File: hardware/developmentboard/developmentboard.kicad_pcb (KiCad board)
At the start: 2 copper layers, 207.5 x 78.1 mm, 39 parts, among them J1 SPI Header, J2 Power Header, J3 Hall Effect Header, U1 ADS7960, U10 DRV5053, U11 DRV5053, U12 DRV5053, U13 DRV5053, U15 REF5025AD, U2 DRV5053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

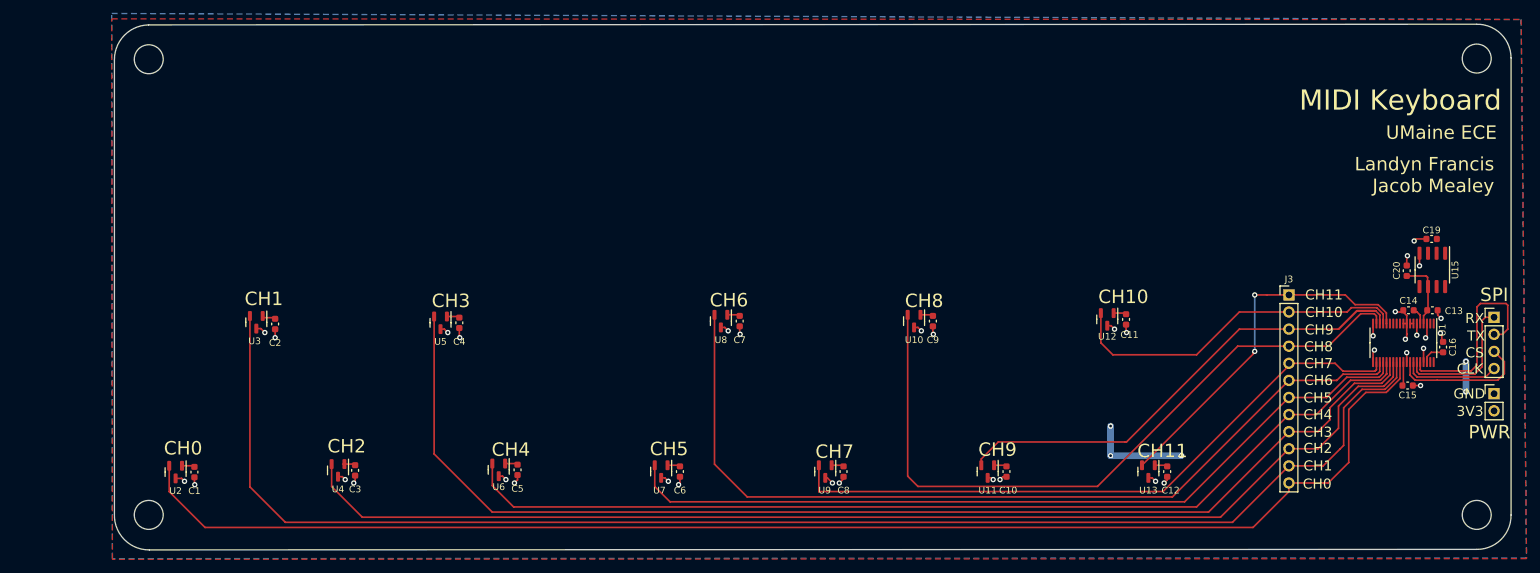
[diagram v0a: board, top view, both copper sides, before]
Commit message: made development board wider, changed reference voltage to use shunt regulator
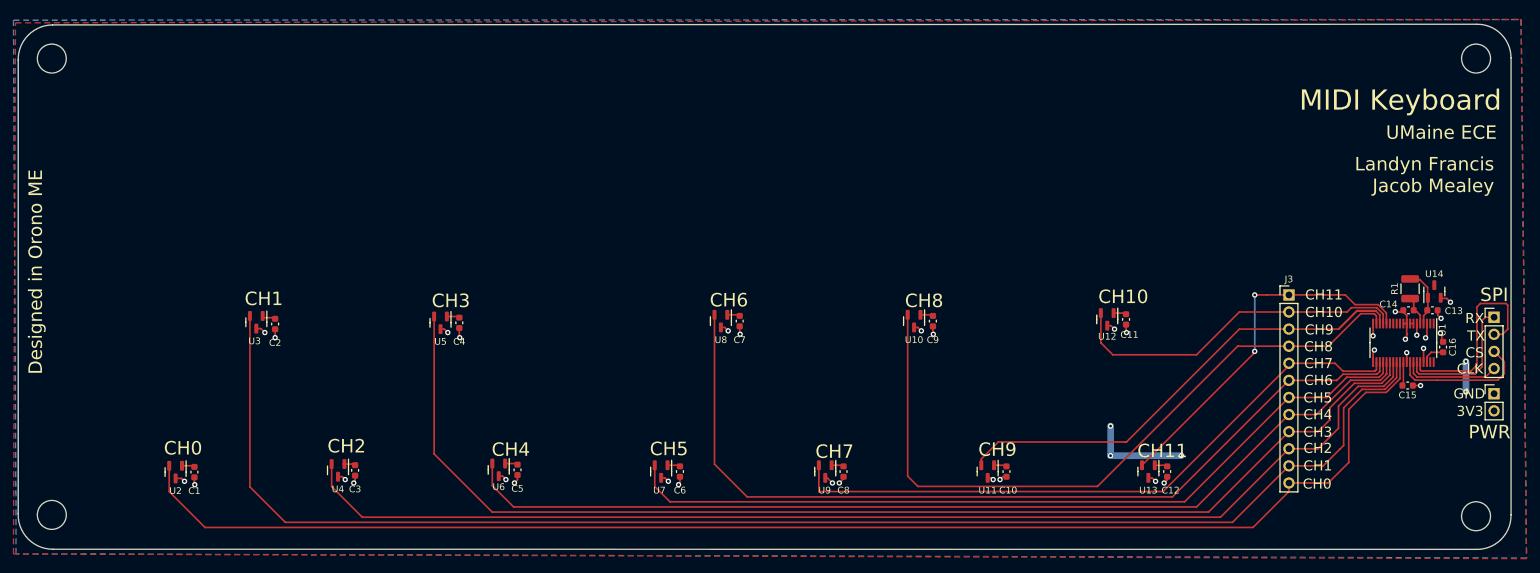
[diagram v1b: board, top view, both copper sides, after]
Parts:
- removed C19: 1-10uF, Capacitor_SMD:C_0603_1608Metric
- removed C20: 1-50uF, Capacitor_SMD:C_0603_1608Metric
- removed the REF** at (58.7, 120.1)
- removed the REF** at (256.0, 120.1)
- removed the REF** at (256.0, 52.3)
- removed the REF** at (58.7, 52.4)
- removed U15: REF5025AD, Package_SO:SOIC-8_3.9x4.9mm_P1.27mm
- added R1: 237, Resistor_SMD:R_1210_3225Metric, F.Cu at (246.1, 86.5)
- added REF**: MountingHole_4.3mm_M4, MountingHole:MountingHole_4.3mm_M4, F.Cu at (44.3, 52.3)
- added REF**: MountingHole_4.3mm_M4, MountingHole:MountingHole_4.3mm_M4, F.Cu at (255.9, 52.3)
- added REF**: MountingHole_4.3mm_M4, MountingHole:MountingHole_4.3mm_M4, F.Cu at (255.9, 120.3)
- added REF**: MountingHole_4.3mm_M4, MountingHole:MountingHole_4.3mm_M4, F.Cu at (44.3, 120.1)
- added U14: LM4040DBZ-2.5, Package_TO_SOT_SMD:SOT-23, F.Cu at (249.7, 86.9)
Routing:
- net GND: track 56.5 -> 52.8 mm, vias 38 -> 36
- net +3.3V: track 51.5 -> 53.3 mm
- net +2V5: track 10.1 -> 8.45 mm
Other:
- board size 207.5 x 78.1 mm -> 221.8 x 78 mm

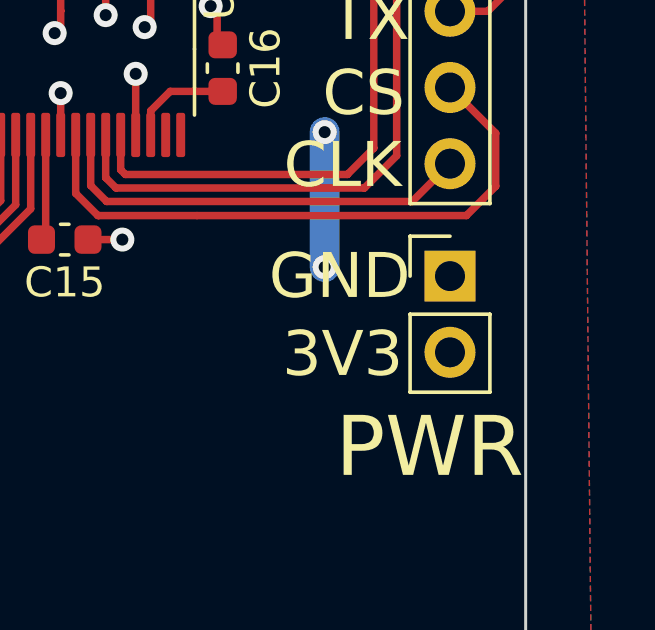
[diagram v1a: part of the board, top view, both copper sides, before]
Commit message: Devboard and Powerboard matching headers lined up
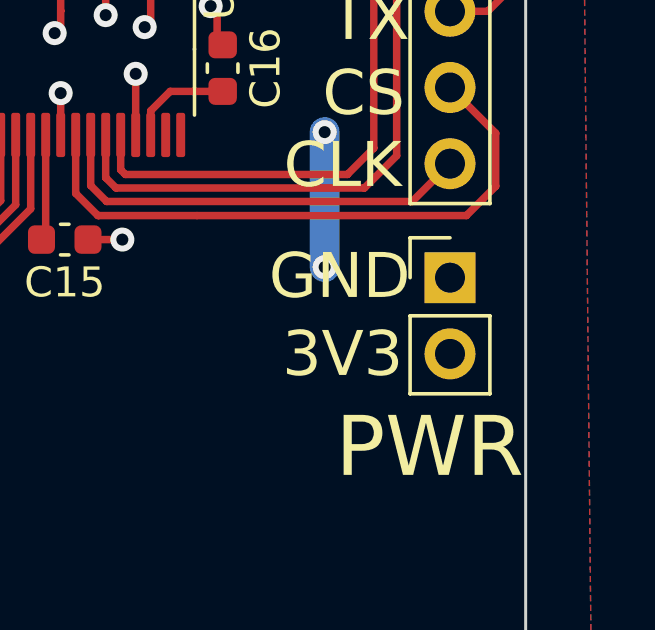
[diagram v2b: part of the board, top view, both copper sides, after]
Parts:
- moved J2 0.05 mm to (258.6, 102.1)
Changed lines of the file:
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@@
     )
   )
-  (footprint "Connector_PinHeader_2.54mm:PinHeader_1x04_P2.54mm_Vertical" (layer "F.Cu")
+  (footprint "Connector_PinHeader_2.54mm:PinHeader_1x04_P2.54mm_Vertical" locked (layer "F.Cu")
     (at 258.572 90.688)
     (descr "Through hole straight pin header, 1x04, 2.54mm pitch, single row")
@@
     (fp_line (start -1.27 -0.635) (end -0.635 -1.27) (layer "F.Fab") (width 0.1))
     (fp_line (start -1.27 8.89) (end -1.27 -0.635) (layer "F.Fab") (width 0.1))
-    (pad "1" thru_hole rect (at 0 0) (size 1.7 1.7) (drill 1) (layers *.Cu *.Mask)
+    (pad "1" thru_hole rect locked (at 0 0) (size 1.7 1.7) (drill 1) (layers *.Cu *.Mask)
       (net 4 "RX") (pinfunction "Pin_1") (pintype "passive"))
-    (pad "2" thru_hole oval (at 0 2.54) (size 1.7 1.7) (drill 1) (layers *.Cu *.Mask)
+    (pad "2" thru_hole oval locked (at 0 2.54) (size 1.7 1.7) (drill 1) (layers *.Cu *.Mask)
       (net 5 "TX") (pinfunction "Pin_2") (pintype "passive"))
-    (pad "3" thru_hole oval (at 0 5.08) (size 1.7 1.7) (drill 1) (layers *.Cu *.Mask)
+    (pad "3" thru_hole oval locked (at 0 5.08) (size 1.7 1.7) (drill 1) (layers *.Cu *.Mask)
       (net 6 "CS") (pinfunction "Pin_3") (pintype "passive"))
-    (pad "4" thru_hole oval (at 0 7.62) (size 1.7 1.7) (drill 1) (layers *.Cu *.Mask)
+    (pad "4" thru_hole oval locked (at 0 7.62) (size 1.7 1.7) (drill 1) (layers *.Cu *.Mask)
       (net 7 "SCLK") (pinfunction "Pin_4") (pintype "passive"))
     (model "${KICAD6_3DMODEL_DIR}/Connector_PinHeader_2.54mm.3dshapes/PinHeader_1x04_P2.54mm_Vertical.wrl"
@@
     )
   )
-  (footprint "Connector_PinHeader_2.54mm:PinHeader_1x02_P2.54mm_Vertical" (layer "F.Cu")
-    (at 258.572 102.056)
+  (footprint "Connector_PinHeader_2.54mm:PinHeader_1x02_P2.54mm_Vertical" locked (layer "F.Cu")
+    (at 258.572 102.108)
     (descr "Through hole straight pin header, 1x02, 2.54mm pitch, single row")
     (tags "Through hole pin header THT 1x02 2.54mm single row")
@@
     (fp_line (start -1.27 -0.635) (end -0.635 -1.27) (layer "F.Fab") (width 0.1))
     (fp_line (start -1.27 3.81) (end -1.27 -0.635) (layer "F.Fab") (width 0.1))
-    (pad "1" thru_hole rect (at 0 0) (size 1.7 1.7) (drill 1) (layers *.Cu *.Mask)
+    (pad "1" thru_hole rect locked (at 0 0) (size 1.7 1.7) (drill 1) (layers *.Cu *.Mask)
       (net 1 "GND") (pinfunction "Pin_1") (pintype "passive"))
-    (pad "2" thru_hole oval (at 0 2.54) (size 1.7 1.7) (drill 1) (layers *.Cu *.Mask)
+    (pad "2" thru_hole oval locked (at 0 2.54) (size 1.7 1.7) (drill 1) (layers *.Cu *.Mask)
       (net 2 "+3.3V") (pinfunction "Pin_2") (pintype "passive"))
     (model "${KICAD6_3DMODEL_DIR}/Connector_PinHeader_2.54mm.3dshapes/PinHeader_1x02_P2.54mm_Vertical.wrl"
@@
     (connect_pads (clearance 0))
     (min_thickness 0.254)
-    (keepout (tracks allowed) (vias allowed) (pads allowed) (copperpour not_allowed) (footprints allowed))
+    (keepout (tracks allowed) (vias allowed) (pads allowed ) (copperpour not_allowed) (footprints allowed))
     (fill (thermal_gap 0.508) (thermal_bridge_width 0.508))
     (polygon
